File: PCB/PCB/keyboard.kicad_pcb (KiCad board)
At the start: 2 copper layers, 368.2 x 122.7 mm, 225 parts, among them SW1 SW_PUSH, SW2 SW_PUSH, U1 STM32F072CBUx, U2 MCP1700-3302E_SOT23, U3 USBLC6-2SC6

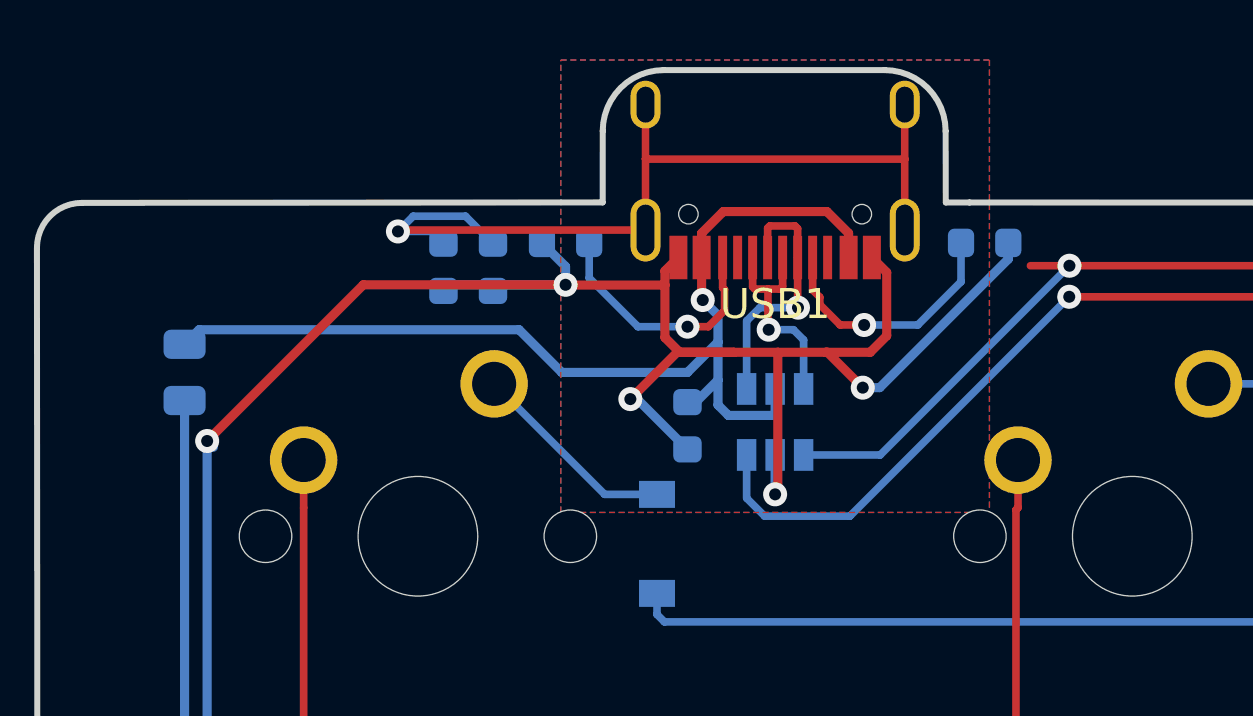
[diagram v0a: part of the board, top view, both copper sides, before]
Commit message: Updated so that USB-C is on the bottom of the PCB again
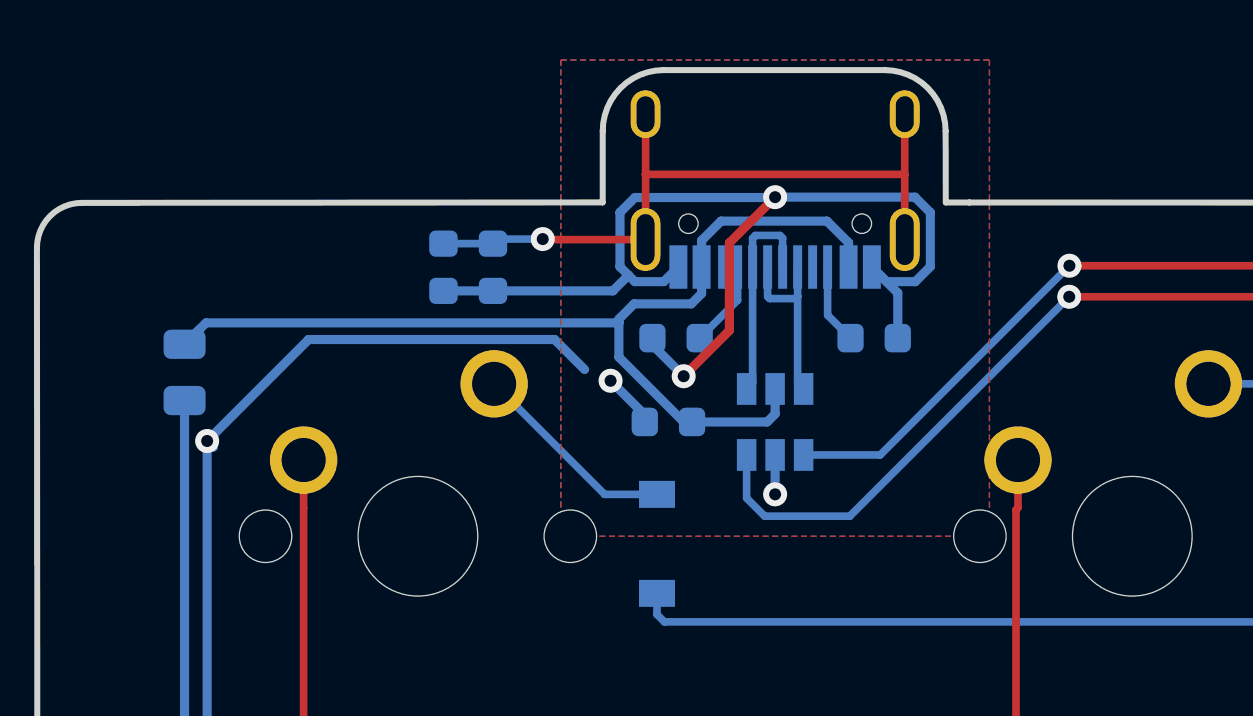
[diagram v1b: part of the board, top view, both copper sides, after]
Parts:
- USB1: moved to B.Cu
- moved R4 10.8 mm to (107.8, 85.5), turned to 180 degrees
- moved R5 10.8 mm to (114.4, 85.5), turned to 0 degrees
- moved C11 0.65 mm to (107.6, 88.3), turned to 0 degrees
- moved USB1 0.32 mm to (111.1, 75.4), turned to 0 degrees
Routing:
- net Net-(C10-Pad2): track 30.7 -> 23.8 mm
- net GND: track 412.1 -> 405.8 mm
- net Net-(R5-Pad1): track 8.37 -> 2.69 mm, vias 1 -> 0
- net Net-(R4-Pad1): track 8.55 -> 2.89 mm, vias 1 -> 0
- net DBus-: track 8.85 -> 7.15 mm, vias 1 -> 0
- net D+: track 279.8 -> 278.5 mm
- net DBus+: track 7.31 -> 6.19 mm, vias 1 -> 0
- net VBUS: track 35.5 -> 34.9 mm, vias 1 -> 0
